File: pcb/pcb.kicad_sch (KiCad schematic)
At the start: 249 parts, among them J1 USB_C_Receptacle_USB2.0, J2 AVR-ISP-6, SW1 1U, SW10 1U, SW100 ISO SHIFT, SW101 2U, SW102 1.25U CTRL, SW103 1.25U GUI, SW104 1.25U ALT, SW105 6.25u SPACE, SW106 1U ALT, SW107 1U GUI, SW108 1U CTRL, SW109 1U, SW11 1U, SW110 1U, SW111 1U, SW112 1U, SW113 1U, SW114 1U, SW115 1.5U CTRL, SW116 1U GUI, SW117 1.5U ALT, SW118 7U SPACE, SW119 1.5U ALT, SW12 1U, SW120 1.5U CTRL, SW121 1.5U GUI, SW122 6U SPACE, SW123 SW_Push, SW124 SW_Push, SW13 1U, SW14 1U, SW15 1U, SW16 1U, SW17 1U, SW18 1U, SW19 1U, SW2 1U, SW20 1U, SW21 1U, SW22 1U, SW23 1U, SW24 1U, SW25 1U, SW26 1U, SW27 1U, SW28 1U, SW29 1U, SW3 1U, SW30 1U, SW31 1U, SW32 1U, SW33 1U, SW34 1U, SW35 1U, SW36 1U, SW37 2U, SW38 1U, SW39 1U, SW4 1U, SW40 1U, SW41 1U, SW42 1U, SW43 1.5U, SW44 1U, SW45 1U, SW46 1U, SW47 1U, SW48 1U, SW49 1U, SW5 1U, SW50 1U, SW51 1U, SW52 1U, SW53 1U, SW54 1U, SW55 1U, SW56 1.5U, SW57 1U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

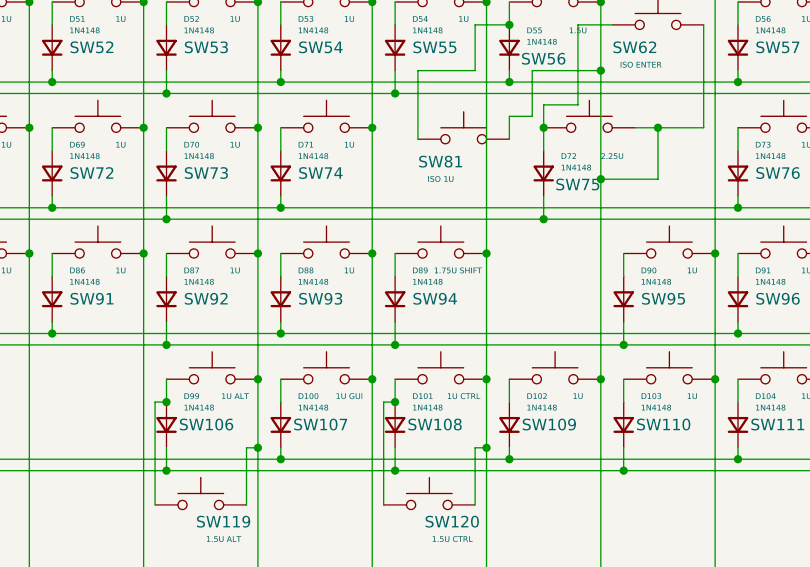
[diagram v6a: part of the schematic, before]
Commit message: Routing rows 7
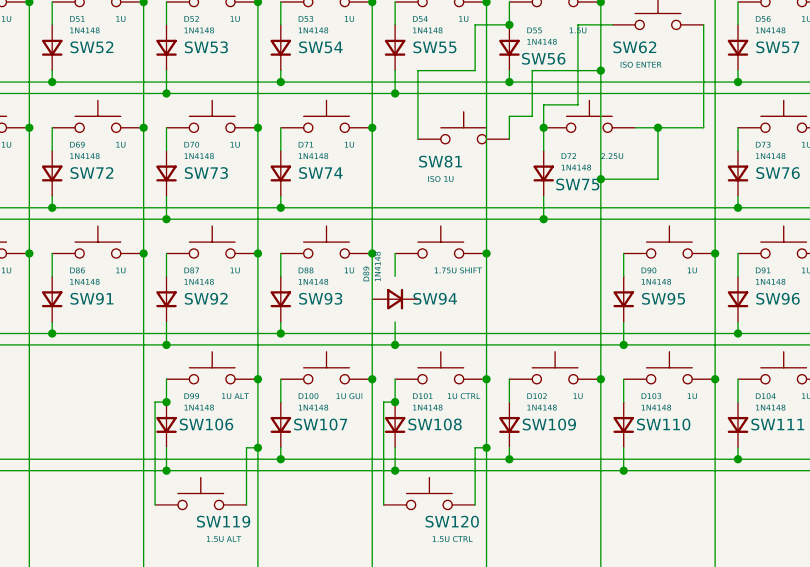
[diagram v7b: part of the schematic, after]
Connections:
- net ROW10: no longer D89.1 (K)
- net at SW94.1: no longer D89.2 (A)
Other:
- moved on the sheet: D89
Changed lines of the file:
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@@
     (pin "2")
   )
-  (symbol (lib_id "Device:D_Small") (at 245.11 118.11 90) (unit 1)
+  (symbol (lib_id "Device:D_Small") (at 245.11 118.11 180) (unit 1)
     (in_bom yes) (on_board yes)
-    (property "Reference" "D89" (id 0) (at 247.015 114.935 90)
+    (property "Reference" "D89" (id 0) (at 241.935 116.205 90)
       (effects (font (size 0.635 0.635)) (justify right))
     )
-    (property "Value" "1N4148" (id 1) (at 247.015 116.205 90)
+    (property "Value" "1N4148" (id 1) (at 243.205 116.205 90)
       (effects (font (size 0.635 0.635)) (justify right))
     )

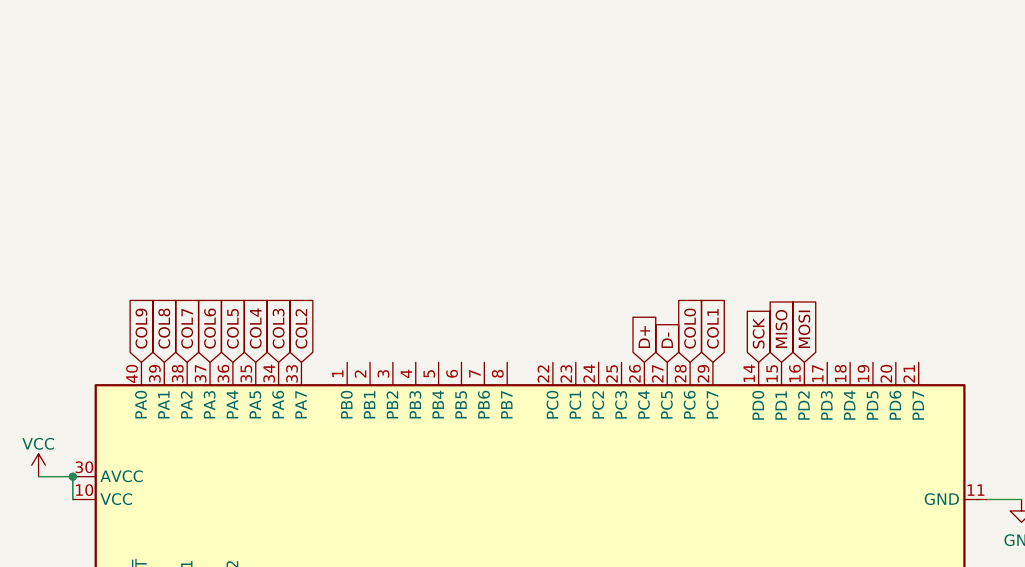
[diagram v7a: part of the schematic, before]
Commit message: Routing more than just rows 1
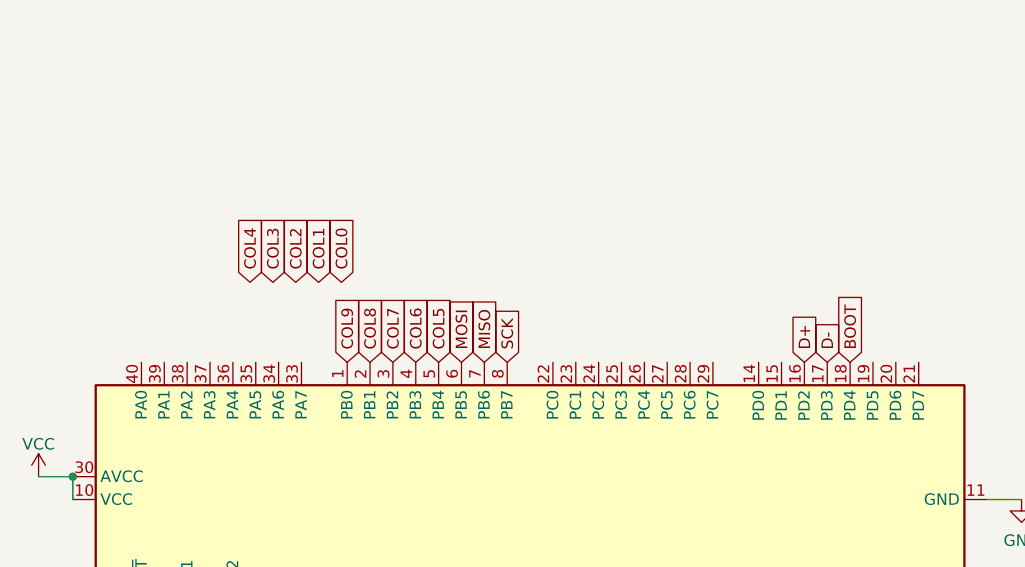
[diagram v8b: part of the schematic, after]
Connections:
- net BOOT: now also U1.18 (PD4)
- net COL0: no longer U1.28 (PC6)
- net COL1: no longer U1.29 (PC7)
- net COL2: no longer U1.33 (PA7)
- net COL3: no longer U1.34 (PA6)
- net COL4: no longer U1.35 (PA5)
- net COL5: now also U1.5 (PB4); no longer U1.36 (PA4)
- net COL6: now also U1.4 (PB3); no longer U1.37 (PA3)
- net COL7: now also U1.3 (PB2); no longer U1.38 (PA2)
- net COL8: now also U1.2 (PB1); no longer U1.39 (PA1)
- net COL9: now also U1.1 (PB0); no longer U1.40 (PA0)
- net D+: now also U1.16 (PD2); no longer U1.26 (PC4)
- net D-: now also U1.17 (PD3); no longer U1.27 (PC5)
- net MISO: now also U1.7 (PB6); no longer U1.15 (PD1)
- net MOSI: now also U1.6 (PB5); no longer U1.16 (PD2)
- net SCK: now also U1.8 (PB7); no longer U1.14 (PD0)
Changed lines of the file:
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@@
     )
   )
-  (global_label "COL9" (shape input) (at 30.48 224.79 90) (fields_autoplaced)
-    (effects (font (size 1.27 1.27)) (justify left))
-    (property "Intersheet References" "${INTERSHEET_REFS}" (id 0) (at 30.4006 217.5388 90)
-      (effects (font (size 1.27 1.27)) (justify left) hide)
-    )
-  )
-  (global_label "SCK" (shape input) (at 99.06 224.79 90) (fields_autoplaced)
-    (effects (font (size 1.27 1.27)) (justify left))
-    (property "Intersheet References" "${INTERSHEET_REFS}" (id 0) (at 98.9806 218.6274 90)
-      (effects (font (size 1.27 1.27)) (justify left) hide)
-    )
-  )
-  (global_label "COL1" (shape input) (at 93.98 224.79 90) (fields_autoplaced)
-    (effects (font (size 1.27 1.27)) (justify left))
-    (property "Intersheet References" "${INTERSHEET_REFS}" (id 0) (at 93.9006 217.5388 90)
-      (effects (font (size 1.27 1.27)) (justify left) hide)
-    )
-  )
-  (global_label "MISO" (shape input) (at 101.6 224.79 90) (fields_autoplaced)
-    (effects (font (size 1.27 1.27)) (justify left))
-    (property "Intersheet References" "${INTERSHEET_REFS}" (id 0) (at 101.5206 217.7807 90)
+  (global_label "COL9" (shape input) (at 53.34 224.79 90) (fields_autoplaced)
+    (effects (font (size 1.27 1.27)) (justify left))
+    (property "Intersheet References" "${INTERSHEET_REFS}" (id 0) (at 53.2606 217.5388 90)
+      (effects (font (size 1.27 1.27)) (justify left) hide)
+    )
+  )
+  (global_label "SCK" (shape input) (at 71.12 224.79 90) (fields_autoplaced)
+    (effects (font (size 1.27 1.27)) (justify left))
+    (property "Intersheet References" "${INTERSHEET_REFS}" (id 0) (at 71.0406 218.6274 90)
+      (effects (font (size 1.27 1.27)) (justify left) hide)
+    )
+  )
+  (global_label "COL1" (shape input) (at 50.165 215.9 90) (fields_autoplaced)
+    (effects (font (size 1.27 1.27)) (justify left))
+    (property "Intersheet References" "${INTERSHEET_REFS}" (id 0) (at 50.0856 208.6488 90)
+      (effects (font (size 1.27 1.27)) (justify left) hide)
+    )
+  )
+  (global_label "MISO" (shape input) (at 68.58 224.79 90) (fields_autoplaced)
+    (effects (font (size 1.27 1.27)) (justify left))
+    (property "Intersheet References" "${INTERSHEET_REFS}" (id 0) (at 68.5006 217.7807 90)
       (effects (font (size 1.27 1.27)) (justify left) hide)
     )
@@
     )
   )
-  (global_label "COL6" (shape input) (at 38.1 224.79 90) (fields_autoplaced)
-    (effects (font (size 1.27 1.27)) (justify left))
-    (property "Intersheet References" "${INTERSHEET_REFS}" (id 0) (at 38.0206 217.5388 90)
+  (global_label "BOOT" (shape input) (at 109.22 224.79 90) (fields_autoplaced)
+    (effects (font (size 1.27 1.27)) (justify left))
+    (property "Intersheet References" "${INTERSHEET_REFS}" (id 0) (at 109.1406 217.4783 90)
+      (effects (font (size 1.27 1.27)) (justify left) hide)
+    )
+  )
+  (global_label "COL6" (shape input) (at 60.96 224.79 90) (fields_autoplaced)
+    (effects (font (size 1.27 1.27)) (justify left))
+    (property "Intersheet References" "${INTERSHEET_REFS}" (id 0) (at 60.8806 217.5388 90)
       (effects (font (size 1.27 1.27)) (justify left) hide)
     )
@@
     )
   )
-  (global_label "COL4" (shape input) (at 43.18 224.79 90) (fields_autoplaced)
-    (effects (font (size 1.27 1.27)) (justify left))
-    (property "Intersheet References" "${INTERSHEET_REFS}" (id 0) (at 43.1006 217.5388 90)
+  (global_label "COL4" (shape input) (at 42.545 215.9 90) (fields_autoplaced)
+    (effects (font (size 1.27 1.27)) (justify left))
+    (property "Intersheet References" "${INTERSHEET_REFS}" (id 0) (at 42.4656 208.6488 90)
       (effects (font (size 1.27 1.27)) (justify left) hide)
     )
@@
     )
   )
-  (global_label "COL2" (shape input) (at 48.26 224.79 90) (fields_autoplaced)
-    (effects (font (size 1.27 1.27)) (justify left))
-    (property "Intersheet References" "${INTERSHEET_REFS}" (id 0) (at 48.1806 217.5388 90)
+  (global_label "COL2" (shape input) (at 47.625 215.9 90) (fields_autoplaced)
+    (effects (font (size 1.27 1.27)) (justify left))
+    (property "Intersheet References" "${INTERSHEET_REFS}" (id 0) (at 47.5456 208.6488 90)
       (effects (font (size 1.27 1.27)) (justify left) hide)
     )
@@
     )
   )
-  (global_label "COL8" (shape input) (at 33.02 224.79 90) (fields_autoplaced)
-    (effects (font (size 1.27 1.27)) (justify left))
-    (property "Intersheet References" "${INTERSHEET_REFS}" (id 0) (at 32.9406 217.5388 90)
-      (effects (font (size 1.27 1.27)) (justify left) hide)
-    )
-  )
-  (global_label "D+" (shape input) (at 86.36 224.79 90) (fields_autoplaced)
-    (effects (font (size 1.27 1.27)) (justify left))
-    (property "Intersheet References" "${INTERSHEET_REFS}" (id 0) (at 86.2806 219.5345 90)
+  (global_label "COL8" (shape input) (at 55.88 224.79 90) (fields_autoplaced)
+    (effects (font (size 1.27 1.27)) (justify left))
+    (property "Intersheet References" "${INTERSHEET_REFS}" (id 0) (at 55.8006 217.5388 90)
+      (effects (font (size 1.27 1.27)) (justify left) hide)
+    )
+  )
+  (global_label "D+" (shape input) (at 104.14 224.79 90) (fields_autoplaced)
+    (effects (font (size 1.27 1.27)) (justify left))
+    (property "Intersheet References" "${INTERSHEET_REFS}" (id 0) (at 104.0606 219.5345 90)
       (effects (font (size 1.27 1.27)) (justify left) hide)
     )
@@
     )
   )
-  (global_label "MOSI" (shape input) (at 104.14 224.79 90) (fields_autoplaced)
-    (effects (font (size 1.27 1.27)) (justify left))
-    (property "Intersheet References" "${INTERSHEET_REFS}" (id 0) (at 104.0606 217.7807 90)
+  (global_label "MOSI" (shape input) (at 66.04 224.79 90) (fields_autoplaced)
+    (effects (font (size 1.27 1.27)) (justify left))
+    (property "Intersheet References" "${INTERSHEET_REFS}" (id 0) (at 65.9606 217.7807 90)
       (effects (font (size 1.27 1.27)) (justify left) hide)
     )
@@
     )
   )
-  (global_label "D-" (shape input) (at 88.9 224.79 90) (fields_autoplaced)
-    (effects (font (size 1.27 1.27)) (justify left))
-    (property "Intersheet References" "${INTERSHEET_REFS}" (id 0) (at 88.8206 219.5345 90)
+  (global_label "D-" (shape input) (at 106.68 224.79 90) (fields_autoplaced)
+    (effects (font (size 1.27 1.27)) (justify left))
+    (property "Intersheet References" "${INTERSHEET_REFS}" (id 0) (at 106.6006 219.5345 90)
       (effects (font (size 1.27 1.27)) (justify left) hide)
     )
@@
     )
   )
-  (global_label "COL7" (shape input) (at 35.56 224.79 90) (fields_autoplaced)
-    (effects (font (size 1.27 1.27)) (justify left))
-    (property "Intersheet References" "${INTERSHEET_REFS}" (id 0) (at 35.4806 217.5388 90)
+  (global_label "COL7" (shape input) (at 58.42 224.79 90) (fields_autoplaced)
+    (effects (font (size 1.27 1.27)) (justify left))
+    (property "Intersheet References" "${INTERSHEET_REFS}" (id 0) (at 58.3406 217.5388 90)
       (effects (font (size 1.27 1.27)) (justify left) hide)
     )
@@
     )
   )
-  (global_label "COL0" (shape input) (at 91.44 224.79 90) (fields_autoplaced)
-    (effects (font (size 1.27 1.27)) (justify left))
-    (property "Intersheet References" "${INTERSHEET_REFS}" (id 0) (at 91.3606 217.5388 90)
+  (global_label "COL0" (shape input) (at 52.705 215.9 90) (fields_autoplaced)
+    (effects (font (size 1.27 1.27)) (justify left))
+    (property "Intersheet References" "${INTERSHEET_REFS}" (id 0) (at 52.6256 208.6488 90)
       (effects (font (size 1.27 1.27)) (justify left) hide)
     )
@@
     )
   )
-  (global_label "COL5" (shape input) (at 40.64 224.79 90) (fields_autoplaced)
-    (effects (font (size 1.27 1.27)) (justify left))
-    (property "Intersheet References" "${INTERSHEET_REFS}" (id 0) (at 40.5606 217.5388 90)
+  (global_label "COL5" (shape input) (at 63.5 224.79 90) (fields_autoplaced)
+    (effects (font (size 1.27 1.27)) (justify left))
+    (property "Intersheet References" "${INTERSHEET_REFS}" (id 0) (at 63.4206 217.5388 90)
       (effects (font (size 1.27 1.27)) (justify left) hide)
     )
@@
     )
   )
-  (global_label "COL3" (shape input) (at 45.72 224.79 90) (fields_autoplaced)
-    (effects (font (size 1.27 1.27)) (justify left))
-    (property "Intersheet References" "${INTERSHEET_REFS}" (id 0) (at 45.6406 217.5388 90)
-      (effects (font (size 1.27 1.27)) (justify left) hide)
-    )
+  (global_label "COL3" (shape input) (at 45.085 215.9 90) (fields_autoplaced)
+    (effects (font (size 1.27 1.27)) (justify left))
+    (property "Intersheet References" "${INTERSHEET_REFS}" (id 0) (at 45.0056 208.6488 90)
+      (effects (font (size 1.27 1.27)) (justify left) hide)
+    )
